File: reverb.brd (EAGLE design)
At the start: 152.4 x 25.4 mm, 59 parts, among them IC2 TL074, IC2_EQ1 NE5532, IC4_DRV_RCVR TL072, T1 2N3904

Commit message: a little more board work
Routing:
- net +12V_B: track 0.00 -> 135.3 mm
- net -12V_B: track 0.00 -> 118.0 mm
- net AUDIO_IN: track 0.00 -> 50.7 mm
- net N$6: track 0.00 -> 48.2 mm
- net REVERB_SEND: track 0.00 -> 43.9 mm
- net SUM: track 0.00 -> 39.3 mm
- net N$5: track 0.00 -> 38.0 mm
- net REVERB_RETURN: track 0.00 -> 31.1 mm
- net X_FADE_IN: track 0.00 -> 30.6 mm
- net N$7: track 0.00 -> 29.3 mm
- net +12V: track 0.00 -> 28.1 mm
- net N$20: track 0.00 -> 27.9 mm
- net N$18: track 0.00 -> 25.1 mm
- net N$4: track 0.00 -> 23.1 mm
- net N$31: track 0.00 -> 21.1 mm
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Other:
- board size 152.4 x 25.4 mm -> 153 x 25.4 mm

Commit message: moved some stuff around.. might need to hook up some gnds still
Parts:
- ATTN, BLND: value (none) -> 50K
- EQ: value (none) -> 10K
- SWITCH: value (none) -> XFADE_OR_REVERB
- moved R7 0.90 mm to (60.3, 21.0)
- moved C10 0.64 mm to (58.4, 18.4)
- moved R16 0.64 mm to (52.1, 1.91)
- moved IC2 0.63 mm to (61.0, 12.1)
- moved R34 0.63 mm to (57.8, 23.5)
- renumbered ATTN_50K to ATTN, AUDIO_IN to IN, AUDIO_OUT to OUT, BLEND_50K to BLND, CV_IN to CV, TILT_EQ10K to EQ, XFADE_REV_SWITCH to SWITCH
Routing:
- net +12V_B: track 135.3 -> 129.2 mm
- net REVERB_SEND: track 43.9 -> 41.1 mm
- net SUM: track 39.3 -> 42.0 mm
- net N$31: track 21.1 -> 18.6 mm
- net X_FADE_IN: track 30.6 -> 28.8 mm
- net -12V_B: track 118.0 -> 118.9 mm
- net MIX_OUT_B: track 16.6 -> 15.9 mm
- net N$15: track 8.56 -> 7.93 mm
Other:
- board size 153 x 25.4 mm -> 152.4 x 25.4 mm
- board text removed: "EQ Section"
- board text removed: "SPRING DRIVE"

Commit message: everything is hooked up and not overlapping!
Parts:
- moved OUT 3.81 mm to (61.6, 1.91), turned to 180 degrees
- moved ATTN 3.18 mm to (34.9, 1.91)
- moved R8 3.17 mm to (70.5, 1.91)
- renumbered LED1 to LED
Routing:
- net GND: track 0.00 -> 27.6 mm
- net MIX_OUT_B: track 15.9 -> 8.94 mm
- net N$20: track 27.7 -> 34.3 mm
- net N$10: track 12.3 -> 15.5 mm
- net -12V_B: track 118.9 -> 122.0 mm, vias 0 -> 1
- net N$15: track 7.93 -> 10.4 mm
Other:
- board text added: "+V"
- board text added: "-V"
- board text added: "GND"

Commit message: added holes, think its ready to send out
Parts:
- moved J1 5.08 mm to (12.7, 12.7)
- moved 0.1A_FUSE 3.58 mm to (10.7, 2.10), turned to 180 degrees
- moved 0.1A_FUSE_2 2.73 mm to (11.1, 23.2), turned to 180 degrees
- moved TO_OUTPUT 2.03 mm to (143.5, 9.21)
- moved D3 1.93 mm to (18.5, 6.99)
- moved R33 1.91 mm to (27.9, 14.0)
- moved T1 1.91 mm to (22.9, 12.7)
- moved D4 1.90 mm to (18.4, 19.1)
- moved BLND 1.59 mm to (31.4, 23.5)
- moved TO_INPUT 1.59 mm to (137.2, 18.1)
- moved C17 1.27 mm to (22.2, 3.17)
- moved C14 0.64 mm to (22.2, 22.2)
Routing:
- net N$36: track 17.1 -> 14.9 mm
- net N$17: track 13.9 -> 12.0 mm
- net N$37: track 12.9 -> 11.3 mm
- net N$7: track 29.3 -> 30.9 mm
- net N$5: track 38.1 -> 39.4 mm
- net +12V_INLET: track 5.17 -> 6.46 mm
- net -12V_INLET: track 5.92 -> 6.71 mm
- net N$4: track 23.1 -> 22.4 mm
- net N$14: track 6.77 -> 6.25 mm

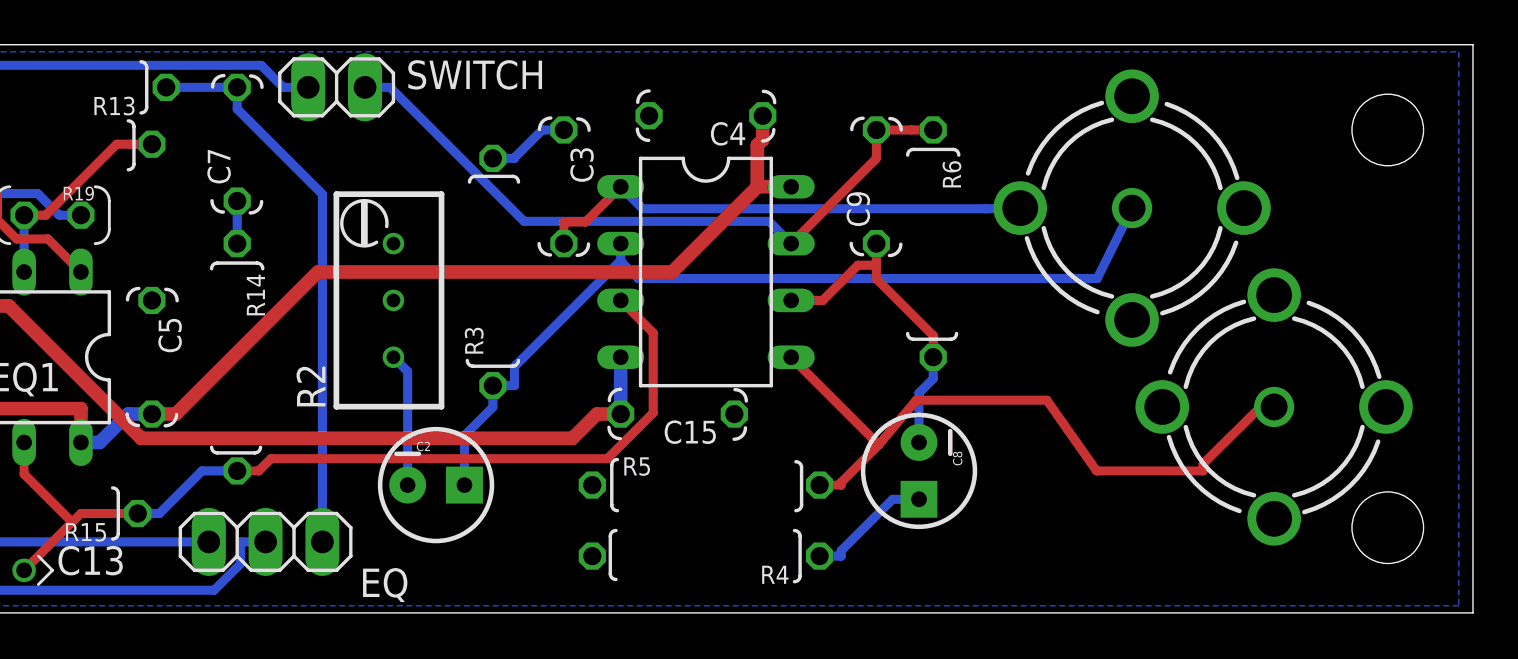
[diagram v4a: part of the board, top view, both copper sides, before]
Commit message: separated out the RCA jacks a bit
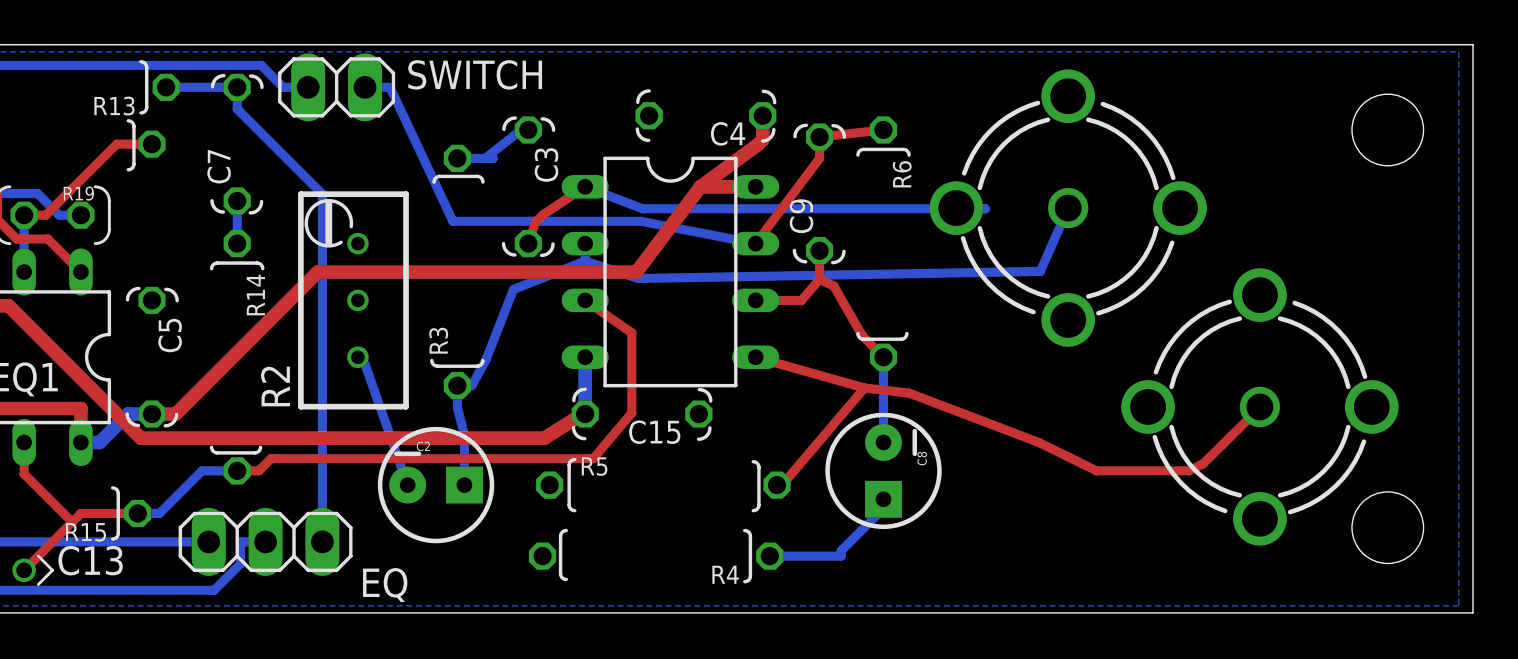
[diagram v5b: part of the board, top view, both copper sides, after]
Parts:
- moved TO_INPUT 2.86 mm to (134.3, 18.1)
- moved C9 2.56 mm to (123.2, 18.7)
- moved R6 2.22 mm to (126.0, 16.5)
- moved R4 2.22 mm to (115.9, 2.54)
- moved R5 1.91 mm to (116.2, 5.71)
- moved C15 1.59 mm to (115.3, 8.89)
- moved C3 1.59 mm to (110.2, 19.1)
- moved C8 1.59 mm to (126.0, 6.35)
- moved IC4_DRV_RCVR 1.59 mm to (116.5, 15.2)
- moved R2 1.59 mm to (102.6, 14.0)
- moved R3 1.59 mm to (107.0, 15.2)
- moved TO_OUTPUT 0.63 mm to (142.9, 9.21)
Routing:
- net N$5: track 39.4 -> 37.6 mm
- net -12V_B: track 122.2 -> 120.5 mm
- net N$9: track 14.7 -> 13.0 mm
- net N$8: track 5.64 -> 7.09 mm
- net REVERB_RETURN: track 31.1 -> 30.0 mm
- net N$4: track 22.4 -> 23.1 mm
- net N$2: track 3.72 -> 4.25 mm
